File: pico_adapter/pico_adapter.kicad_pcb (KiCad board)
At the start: 2 copper layers, 73.9 x 89.2 mm, 46 parts, among them J1 L77HDE15SD1CH4F, J2 AudioJack3, J4 ADD-ON, J5 AGND, J6 PWR_REF, Q1 Q_NMOS_DGS, Q2 Q_NMOS_DGS, SW1 SW_Push

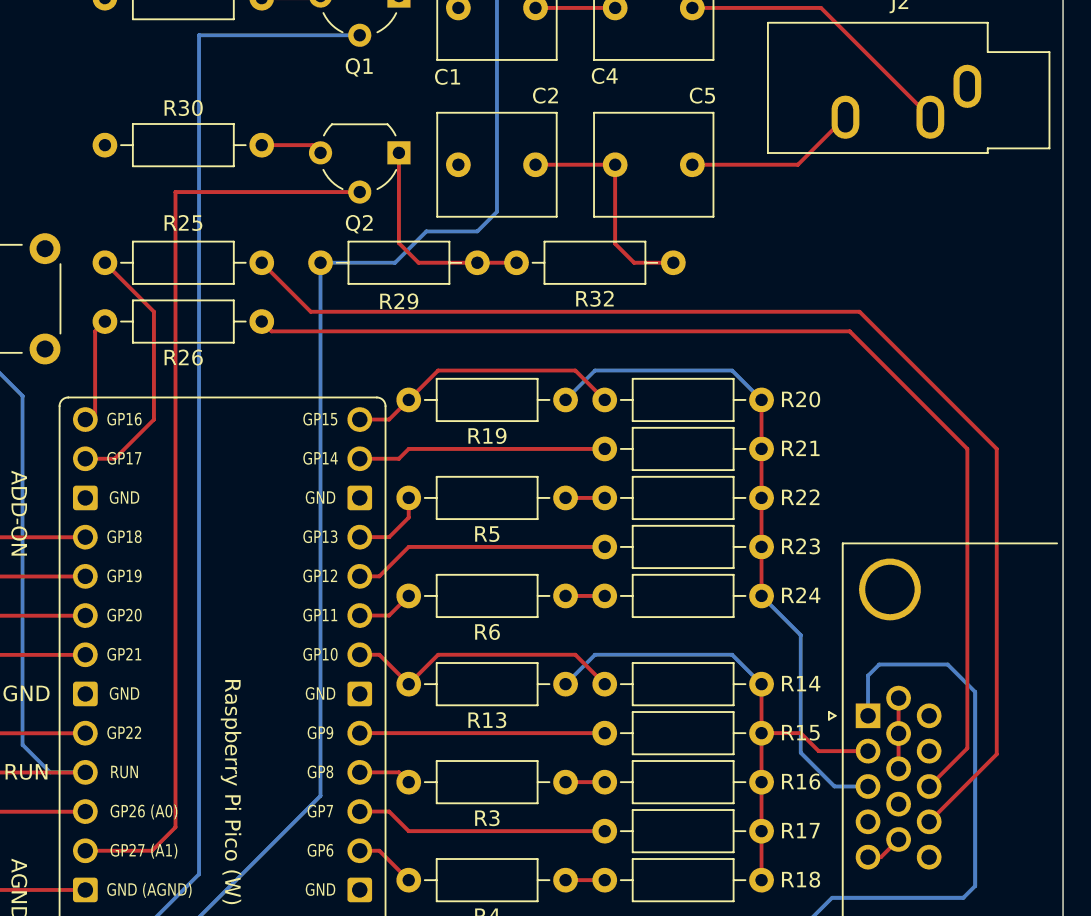
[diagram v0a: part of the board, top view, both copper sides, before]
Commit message: minor changes in layout + added image to readme
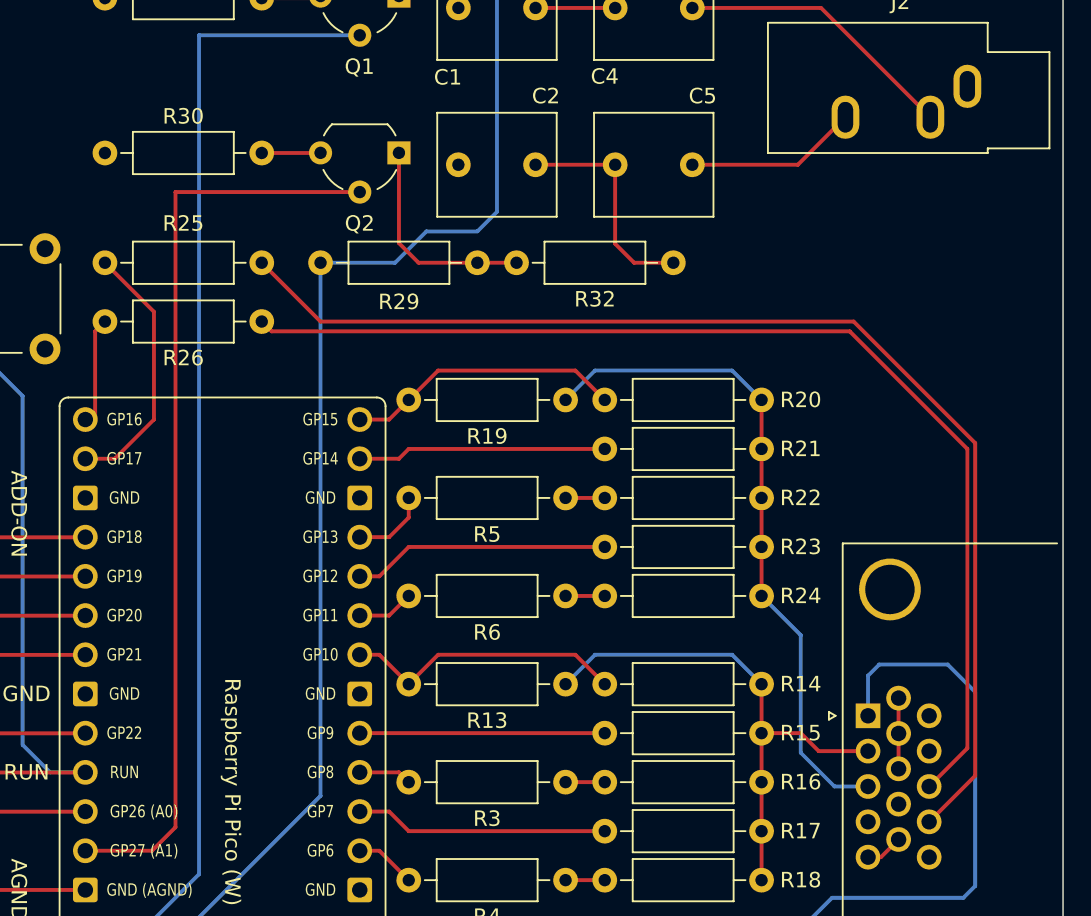
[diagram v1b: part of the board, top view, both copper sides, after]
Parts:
- moved R30 0.51 mm to (45.7, 65.3)
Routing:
- net /VSYNC: track 78.6 -> 76.8 mm
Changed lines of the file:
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@@
   )
   (footprint "Resistor_THT:R_Axial_DIN0207_L6.3mm_D2.5mm_P10.16mm_Horizontal" (layer "F.Cu")
-    (at 45.72 64.77)
+    (at 45.72 65.278)
     (descr "Resistor, Axial_DIN0207 series, Axial, Horizontal, pin pitch=10.16mm, 0.25W = 1/4W, length*diameter=6.3*2.5mm^2, http://cdn-reichelt.de/documents/datenblatt/B400/1_4W%23YAG.pdf")
     (tags "Resistor Axial_DIN0207 series Axial Horizontal pin pitch 10.16mm 0.25W = 1/4W length 6.3mm diameter 2.5mm")
@@
   (segment (start 101.6 84.455) (end 101.6 103.849669) (width 0.25) (layer "F.Cu") (net 43))
   (segment (start 93.98 76.835) (end 101.6 84.455) (width 0.25) (layer "F.Cu") (net 43))
-  (segment (start 94.615 75.565) (end 103.505 84.455) (width 0.25) (layer "F.Cu") (net 44))
-  (segment (start 103.505 104.234669) (end 99.124669 108.615) (width 0.25) (layer "F.Cu") (net 44))
-  (segment (start 59.055 75.565) (end 94.615 75.565) (width 0.25) (layer "F.Cu") (net 44))
-  (segment (start 55.88 72.39) (end 59.055 75.565) (width 0.25) (layer "F.Cu") (net 44))
-  (segment (start 103.505 84.455) (end 103.505 104.234669) (width 0.25) (layer "F.Cu") (net 44))
+  (segment (start 55.88 72.39) (end 59.69 76.2) (width 0.25) (layer "F.Cu") (net 44))
+  (segment (start 59.69 76.2) (end 94.234 76.2) (width 0.25) (layer "F.Cu") (net 44))
+  (segment (start 102.108 84.074) (end 102.108 105.631669) (width 0.25) (layer "F.Cu") (net 44))
+  (segment (start 94.234 76.2) (end 102.108 84.074) (width 0.25) (layer "F.Cu") (net 44))
+  (segment (start 102.108 105.631669) (end 99.124669 108.615) (width 0.25) (layer "F.Cu") (net 44))
   (segment (start 69.215 49.53) (end 65.405 49.53) (width 0.25) (layer "F.Cu") (net 46))
   (segment (start 64.77 50.165) (end 64.77 55.11) (width 0.25) (layer "F.Cu") (net 46))
@@
   (segment (start 64.77 71.12) (end 66.04 72.39) (width 0.25) (layer "F.Cu") (net 48))
   (segment (start 66.04 72.39) (end 69.85 72.39) (width 0.25) (layer "F.Cu") (net 48))
-  (segment (start 55.88 64.77) (end 59.19 64.77) (width 0.25) (layer "F.Cu") (net 49))
-  (segment (start 59.19 64.77) (end 59.69 65.27) (width 0.25) (layer "F.Cu") (net 49))
+  (segment (start 55.88 65.278) (end 59.682 65.278) (width 0.25) (layer "F.Cu") (net 49))
+  (segment (start 59.682 65.278) (end 59.69 65.27) (width 0.25) (layer "F.Cu") (net 49))
   (segment (start 75.565 124.46) (end 78.105 124.46) (width 0.25) (layer "F.Cu") (net 50))
   (segment (start 75.565 130.81) (end 78.105 130.81) (width 0.25) (layer "F.Cu") (net 51))

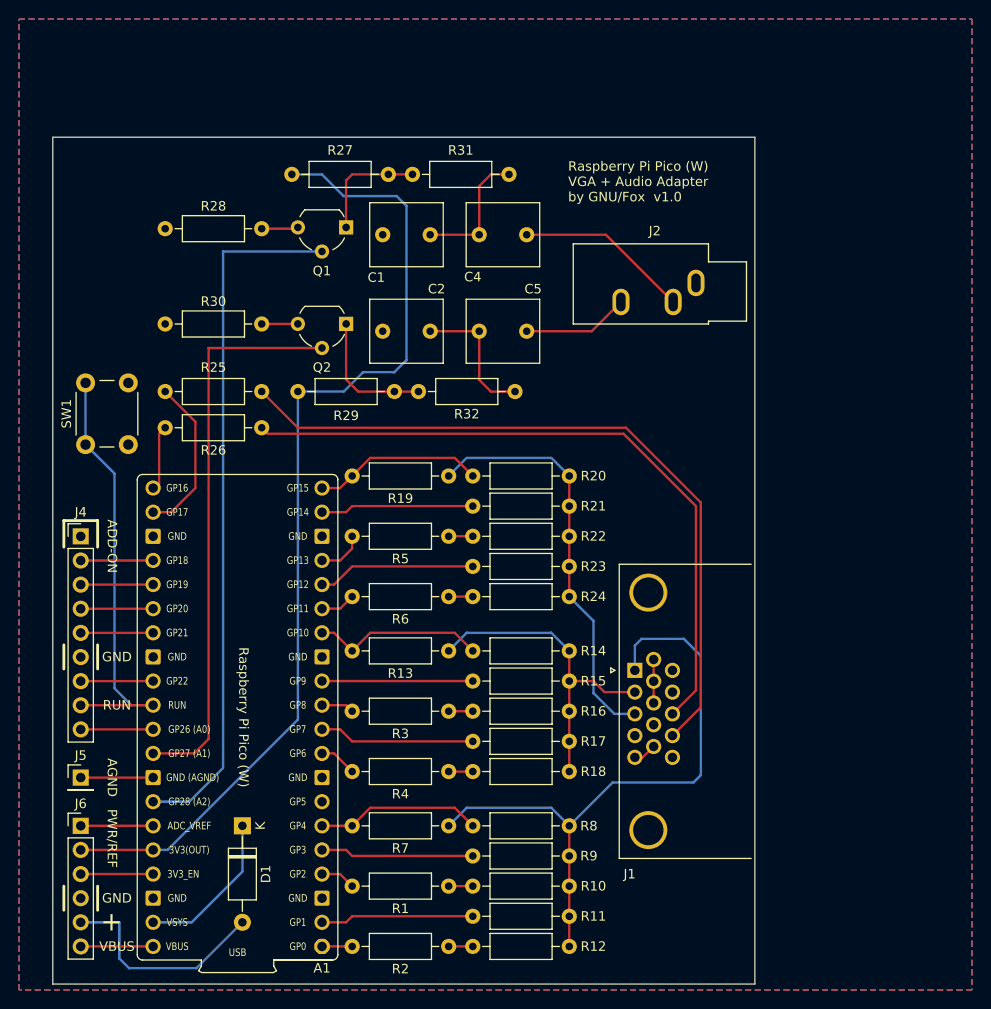
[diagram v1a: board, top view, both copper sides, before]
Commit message: changed VGA connector to more widely available variant + adjusted pcb design rules to JLC-PCB values
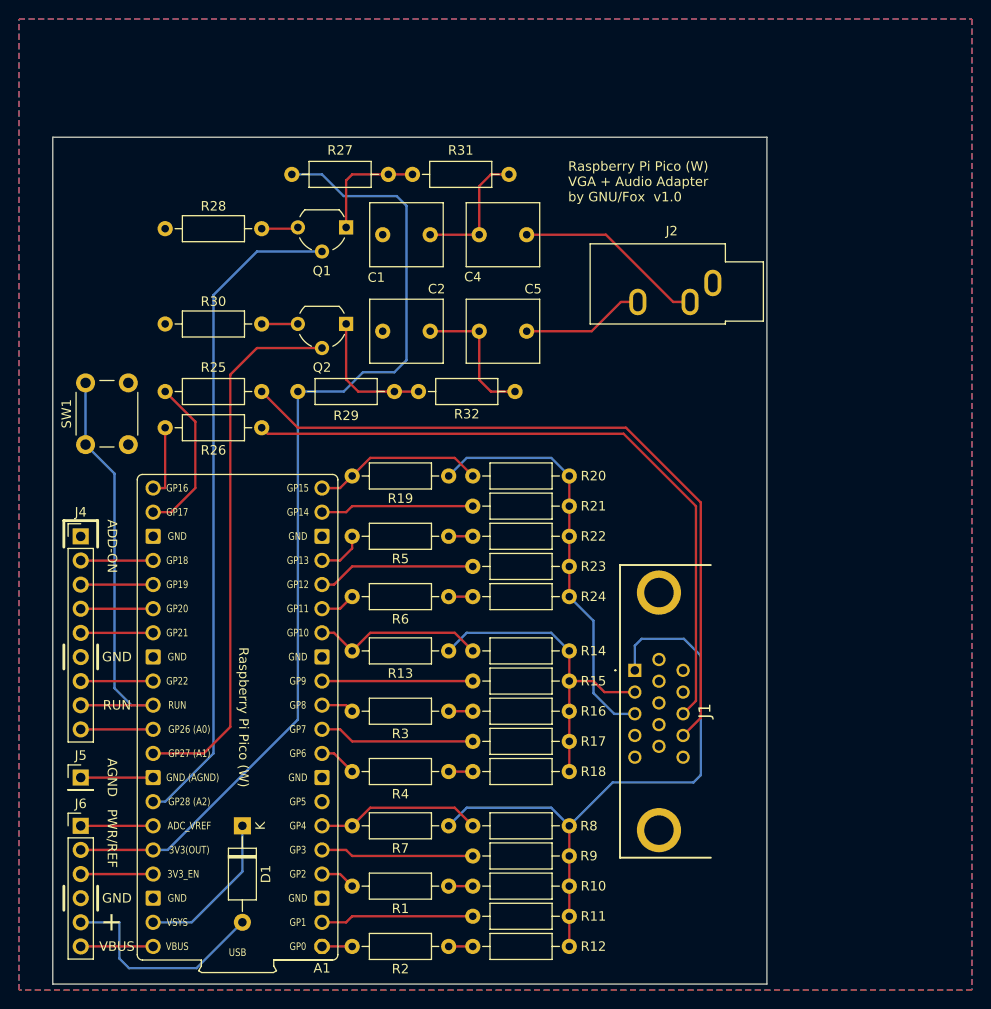
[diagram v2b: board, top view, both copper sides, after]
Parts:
- J1: value L77HDE15SD1CH4F -> VGA_Conn; footprint Connector_Dsub:DSUB-15-HD_Female_Horizontal_P2.29x1.98mm_EdgePinOffset8.35mm_Housed_MountingHolesOffset10.89mm -> VGA_connector:ICD15S13E4GV00LF
- moved J2 1.78 mm to (103.4, 61.0)
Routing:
- net GND: track 7.03 -> 0.00 mm
- net /PWM_L: track 73.6 -> 70.0 mm
- net /PWM_R: track 59.6 -> 57.2 mm
- net Net-(C5-Pad1): track 11.2 -> 13.0 mm
- net Net-(C4-Pad2): track 18.4 -> 20.1 mm
- net /GPIO16: track 6.61 -> 7.62 mm
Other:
- board size 73.9 x 89.2 mm -> 75.2 x 89.2 mm

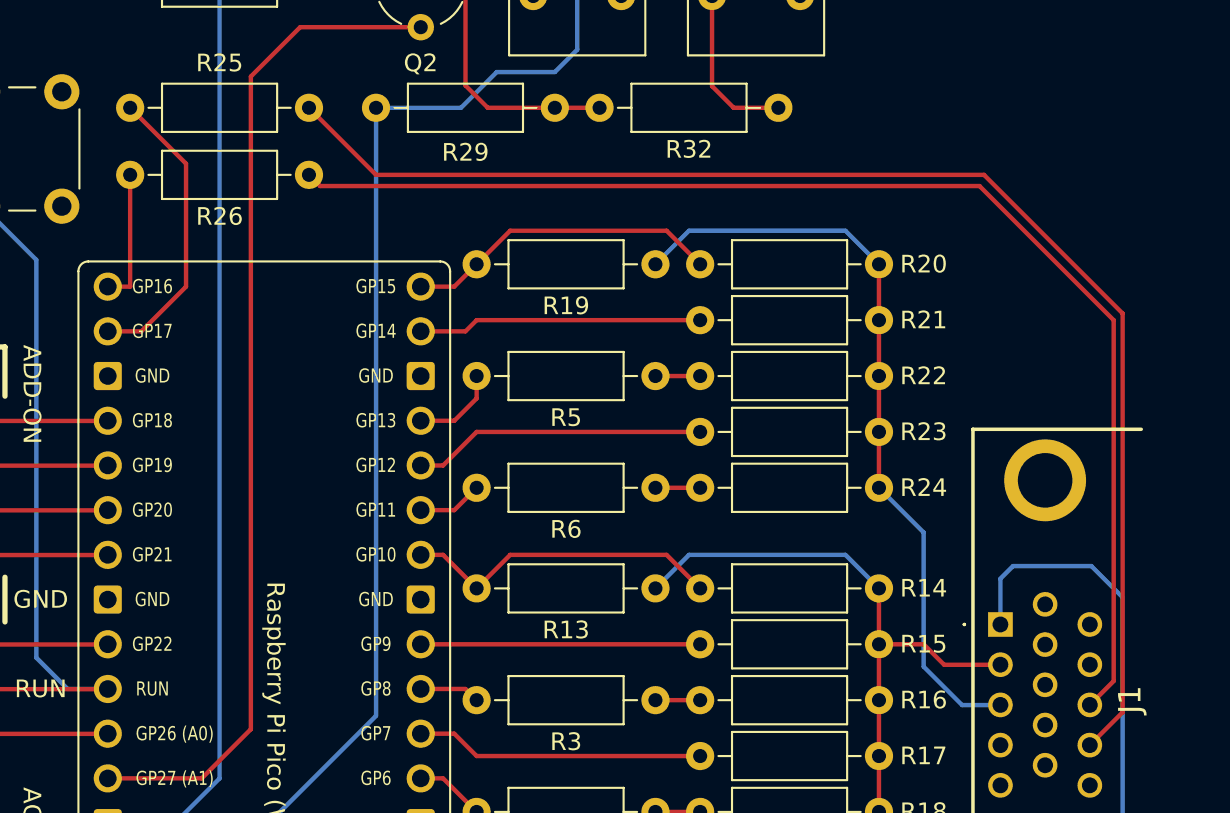
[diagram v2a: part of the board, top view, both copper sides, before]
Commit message: cleaned up some traces
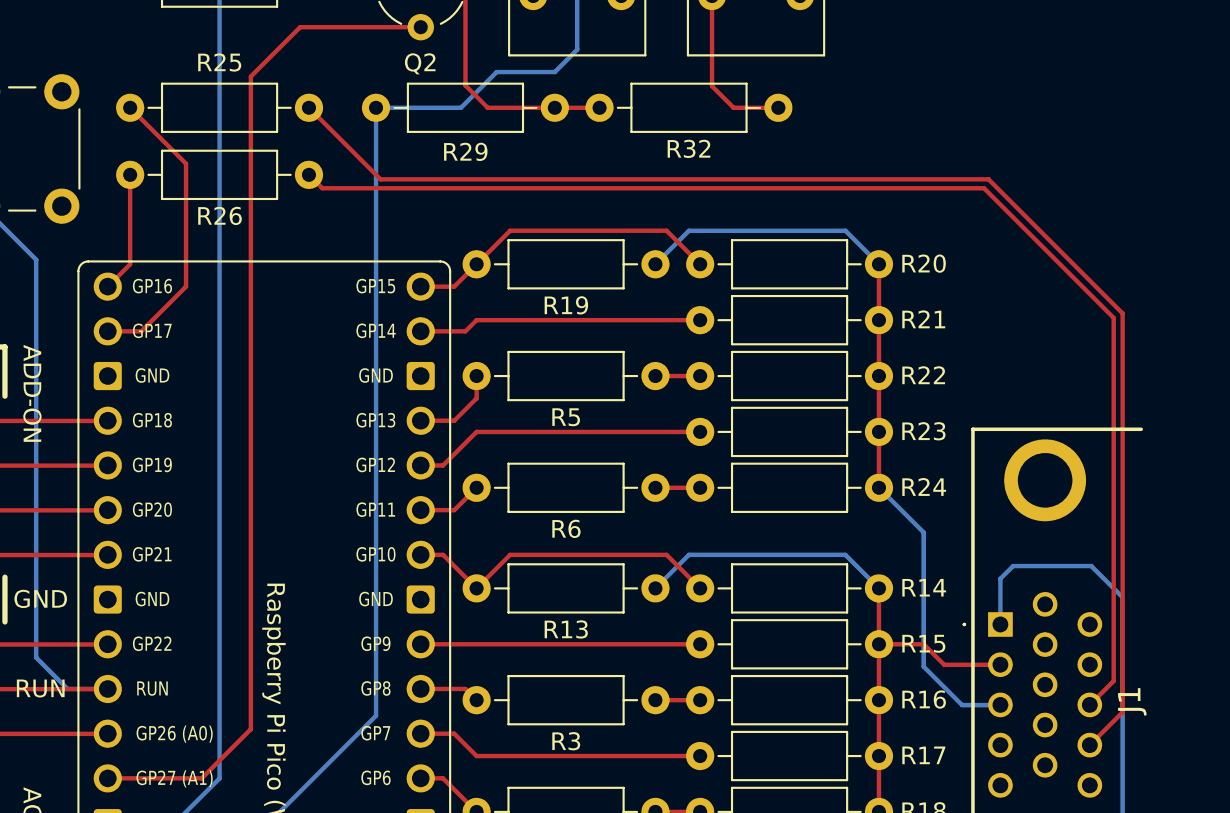
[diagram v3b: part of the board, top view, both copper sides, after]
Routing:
- net /GPIO16: track 7.62 -> 6.88 mm
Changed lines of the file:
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@@
   (segment (start 75.565 81.28) (end 77.47 79.375) (width 0.25) (layer "B.Cu") (net 38))
   (segment (start 86.36 79.375) (end 88.265 81.28) (width 0.25) (layer "B.Cu") (net 38))
-  (segment (start 56.515 76.835) (end 93.98 76.835) (width 0.25) (layer "F.Cu") (net 43))
-  (segment (start 55.88 76.2) (end 56.515 76.835) (width 0.25) (layer "F.Cu") (net 43))
-  (segment (start 101.6 104.959669) (end 100.244669 106.315) (width 0.25) (layer "F.Cu") (net 43))
-  (segment (start 93.98 76.835) (end 101.6 84.455) (width 0.25) (layer "F.Cu") (net 43))
-  (segment (start 101.6 84.455) (end 101.6 104.959669) (width 0.25) (layer "F.Cu") (net 43))
-  (segment (start 59.69 76.2) (end 94.234 76.2) (width 0.25) (layer "F.Cu") (net 44))
+  (segment (start 100.244669 106.315) (end 101.6 104.959669) (width 0.25) (layer "F.Cu") (net 43))
+  (segment (start 101.6 104.959669) (end 101.6 84.328) (width 0.25) (layer "F.Cu") (net 43))
+  (segment (start 56.642 76.962) (end 55.88 76.2) (width 0.25) (layer "F.Cu") (net 43))
+  (segment (start 94.234 76.962) (end 56.642 76.962) (width 0.25) (layer "F.Cu") (net 43))
+  (segment (start 101.6 84.328) (end 94.234 76.962) (width 0.25) (layer "F.Cu") (net 43))
+  (segment (start 102.108 84.074) (end 102.108 106.736669) (width 0.25) (layer "F.Cu") (net 44))
   (segment (start 102.108 106.736669) (end 100.244669 108.6) (width 0.25) (layer "F.Cu") (net 44))
-  (segment (start 102.108 84.074) (end 102.108 106.736669) (width 0.25) (layer "F.Cu") (net 44))
-  (segment (start 55.88 72.39) (end 59.69 76.2) (width 0.25) (layer "F.Cu") (net 44))
-  (segment (start 94.234 76.2) (end 102.108 84.074) (width 0.25) (layer "F.Cu") (net 44))
+  (segment (start 55.88 72.39) (end 59.944 76.454) (width 0.25) (layer "F.Cu") (net 44))
+  (segment (start 94.488 76.454) (end 102.108 84.074) (width 0.25) (layer "F.Cu") (net 44))
+  (segment (start 59.944 76.454) (end 94.488 76.454) (width 0.25) (layer "F.Cu") (net 44))
   (segment (start 69.215 49.53) (end 65.405 49.53) (width 0.25) (layer "F.Cu") (net 46))
   (segment (start 64.77 50.165) (end 64.77 55.11) (width 0.25) (layer "F.Cu") (net 46))
@@
   (segment (start 48.895 75.565) (end 45.72 72.39) (width 0.25) (layer "F.Cu") (net 57))
   (segment (start 48.895 82.55) (end 48.895 75.565) (width 0.25) (layer "F.Cu") (net 57))
-  (segment (start 44.45 82.55) (end 45.72 82.55) (width 0.25) (layer "F.Cu") (net 59))
-  (segment (start 45.72 82.55) (end 45.72 76.2) (width 0.25) (layer "F.Cu") (net 59))
+  (segment (start 44.45 82.55) (end 45.72 81.28) (width 0.25) (layer "F.Cu") (net 59))
+  (segment (start 45.72 81.28) (end 45.72 76.2) (width 0.25) (layer "F.Cu") (net 59))
   (zone (net 58) (net_name "GND") (layers F&B.Cu) (hatch edge 0.508)
     (connect_pads (clearance 0.508))
